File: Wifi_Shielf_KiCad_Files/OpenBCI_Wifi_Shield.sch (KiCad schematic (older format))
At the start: 32 parts, among them P1 CONN_01X04, P10 CONN_01X04, P2 CONN_01X04, P4 CONN_01X02, P5 CONN_01X02, P6 CONN_01X02, P7 CONN_01X08, P8 CONN_01X08, P9 CONN_01X04, SW1 TACT_SWITCH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

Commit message: Aproveitamento do ESP-12E
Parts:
- removed U3: ESP32-WROOM-32, RF_Module:ESP32-WROOM-32, symbol RF_Module:ESP32-WROOM-32
- added IC?: REF200AU, SOIC127P600X175-8N, symbol REF200AU:REF200AU
- added IC?: CD4066BE, DIP794W53P254L1930H508Q14N, symbol CD4066BE:CD4066BE
- added J?: Conn_4x1_HDTDCS, symbol Connector:Conn_01x05_Female
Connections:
- net GND: now also IC?.7 (VSS)
- net C_C: now reaches U1.13 (GPIO4)
- net C_C: now also IC?.6 (CONTROL_C)
- net C_A: now reaches U1.19 (GPIO9)
- net C_A: now also IC?.13 (CONTROL_A)
- net C_B: now reaches U1.20 (GPIO10)
- net C_B: now also IC?.5 (CONTROL_B)
- new net 9V: IC?.14 (VDD), IC?.4 (MIRROR_OUTPUT), IC?.7 (I2_HIGH), IC?.8 (I1_HIGH)
- new net A_OUT: IC?.2 (SIG_A_OUT/IN)
- new net B_OUT: IC?.4 (SIG_B_IN/OUT), IC?.5 (MIRROR_INPUT), IC?.8 (SIG_C_IN/OUT)
- new net COMM: IC?.3 (MIRROR_COMMON)
- new net I1: IC?.1 (I1_LOW), IC?.1 (SIG_A_IN/OUT), IC?.9 (SIG_C_OUT/IN)
- new net I2: IC?.2 (I2_LOW), IC?.3 (SIG_B_OUT/IN)
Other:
- note added: "CURRENT SOURCE"
- moved on the sheet: C1, C2, C3, C4, D1, D2, D3, D4, P1, P10, P2, P4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

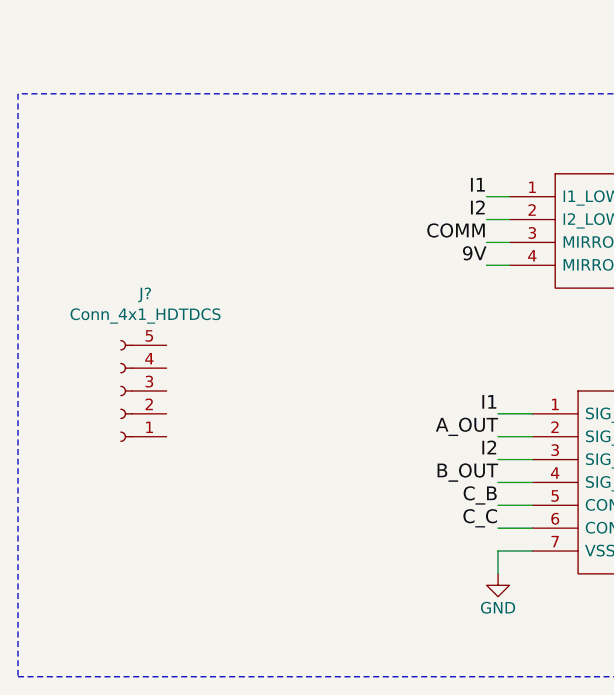
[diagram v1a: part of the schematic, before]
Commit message: Add dos conectores no esquemático de tdcs
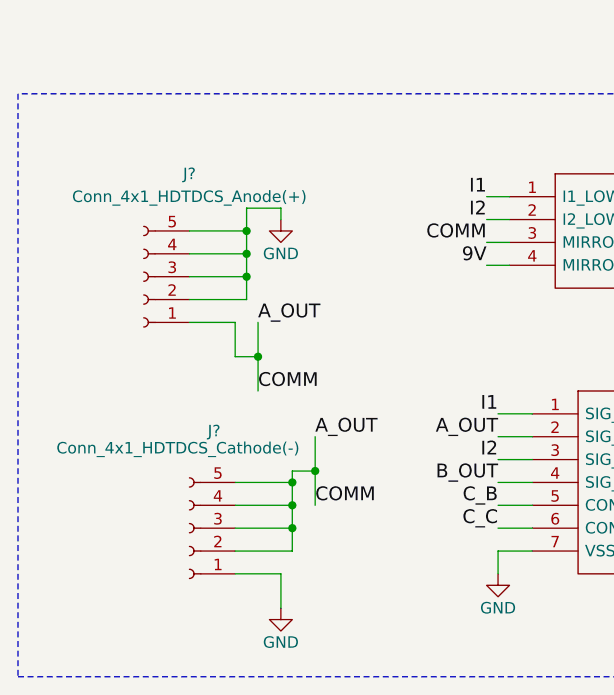
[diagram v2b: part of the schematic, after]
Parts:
- added J?: Conn_4x1_HDTDCS_Anode(+), symbol Connector:Conn_01x05_Female
- J?: value Conn_4x1_HDTDCS -> Conn_4x1_HDTDCS_Cathode(-)
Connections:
- net COMM is gone; now on net A_OUT: IC?.3 (MIRROR_COMMON)
- net A_OUT: now also J?.2 (Pin_2), J?.3 (Pin_3), J?.4 (Pin_4), J?.5 (Pin_5), J?.1 (Pin_1)
- net GND: now also J?.1 (Pin_1), J?.2 (Pin_2), J?.3 (Pin_3), J?.4 (Pin_4), J?.5 (Pin_5)
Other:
- moved on the sheet: J?
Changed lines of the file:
@@
 L Connector:Conn_01x05_Female J?
 U 1 1 631EBAD7
-P 4400 8550
-F 0 "J?" H 4292 8125 50  0000 C CNN
-F 1 "Conn_4x1_HDTDCS" H 4292 8216 50  0000 C CNN
-F 2 "" H 4400 8550 50  0001 C CNN
-F 3 "~" H 4400 8550 50  0001 C CNN
-	1    4400 8550
+P 4700 9150
+F 0 "J?" H 4592 8725 50  0000 C CNN
+F 1 "Conn_4x1_HDTDCS_Cathode(-)" H 4750 8800 50  0000 C CNN
+F 2 "" H 4700 9150 50  0001 C CNN
+F 3 "~" H 4700 9150 50  0001 C CNN
+	1    4700 9150
 	-1   0    0    1
 $EndComp
+$Comp
+L power:GND #PWR?
+U 1 1 6317ABCD
+P 5100 9500
+F 0 "#PWR?" H 5100 9250 50  0001 C CNN
+F 1 "GND" H 5100 9350 50  0000 C CNN
+F 2 "" H 5100 9500 50  0000 C CNN
+F 3 "" H 5100 9500 50  0000 C CNN
+	1    5100 9500
+	1    0    0    -1
+$EndComp
+Wire Wire Line
+	4900 9350 5100 9350
+Wire Wire Line
+	5100 9350 5100 9500
+Text Label 5250 8750 0    60   ~ 0
+A_OUT
+Text Label 5250 9050 0    60   ~ 0
+COMM
+Wire Wire Line
+	5150 8900 5250 8900
+Wire Wire Line
+	5250 8900 5250 8750
+Wire Wire Line
+	5250 9050 5250 8900
+Connection ~ 5250 8900
+Wire Wire Line
+	5150 9250 5150 9150
+Connection ~ 5150 9150
+Wire Wire Line
+	5150 9150 5150 9050
+Connection ~ 5150 9050
+Wire Wire Line
+	5150 9050 5150 8950
+Connection ~ 5150 8950
+Wire Wire Line
+	5150 8950 5150 8900
+Wire Wire Line
+	4900 9250 5150 9250
+Wire Wire Line
+	4900 9150 5150 9150
+Wire Wire Line
+	4900 9050 5150 9050
+Wire Wire Line
+	4900 8950 5150 8950
+$Comp
+L Connector:Conn_01x05_Female J?
+U 1 1 632256B4
+P 4500 8050
+F 0 "J?" H 4300 7600 50  0000 C CNN
+F 1 "Conn_4x1_HDTDCS_Anode(+)" H 4300 7700 50  0000 C CNN
+F 2 "" H 4500 8050 50  0001 C CNN
+F 3 "~" H 4500 8050 50  0001 C CNN
+	1    4500 8050
+	-1   0    0    1
+$EndComp
+$Comp
+L power:GND #PWR?
+U 1 1 632256BA
+P 5100 7800
+F 0 "#PWR?" H 5100 7550 50  0001 C CNN
+F 1 "GND" H 5100 7650 50  0000 C CNN
+F 2 "" H 5100 7800 50  0000 C CNN
+F 3 "" H 5100 7800 50  0000 C CNN
+	1    5100 7800
+	1    0    0    -1
+$EndComp
+Wire Wire Line
+	4700 8250 4900 8250
+Wire Wire Line
+	4900 8250 4900 8400
+Text Label 5000 8250 0    60   ~ 0
+A_OUT
+Text Label 5000 8550 0    60   ~ 0
+COMM
+Wire Wire Line
+	4900 8400 5000 8400
+Wire Wire Line
+	5000 8400 5000 8250
+Wire Wire Line
+	5000 8550 5000 8400
+Connection ~ 5000 8400
+Wire Wire Line
+	4950 8150 4950 8050
+Connection ~ 4950 8050
+Wire Wire Line
+	4950 8050 4950 7950
+Connection ~ 4950 7950
+Wire Wire Line
+	4950 7950 4950 7850
+Connection ~ 4950 7850
+Wire Wire Line
+	4700 8150 4950 8150
+Wire Wire Line
+	4700 8050 4950 8050
+Wire Wire Line
+	4700 7950 4950 7950
+Wire Wire Line
+	4700 7850 4950 7850
+Wire Wire Line
+	4950 7750 5100 7750
+Wire Wire Line
+	5100 7750 5100 7800
+Wire Wire Line
+	4950 7750 4950 7850
 $EndSCHEMATC

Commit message: Adição dos gerber files e layout da pcb
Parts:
- J? (x2): footprint (none) -> Connector_PinHeader_2.54mm:PinHeader_1x05_P2.54mm_Vertical
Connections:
- net 9V is gone; now on net 6V: IC?.14 (VDD), IC?.4 (MIRROR_OUTPUT), IC?.7 (I2_HIGH), IC?.8 (I1_HIGH)
- net 6V: now reaches R2.1, SW3.1 (T), U2.1 (IN)
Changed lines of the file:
@@
 $EndComp
 Wire Wire Line
-	6850 2300 7200 2300
+	6850 2300 7050 2300
 Wire Wire Line
 	8200 3550 8550 3550
@@
 COMM
 Text Label 6000 8000 2    60   ~ 0
-9V
+6V
 Text Label 8150 7500 0    60   ~ 0
-9V
+6V
 Wire Wire Line
 	8100 7800 8150 7800
@@
 	6050 8650 6200 8650
 Text Label 8250 8650 0    60   ~ 0
-9V
+6V
 Wire Wire Line
 	8100 8650 8250 8650
@@
 F 0 "J?" H 4592 8725 50  0000 C CNN
 F 1 "Conn_4x1_HDTDCS_Cathode(-)" H 4750 8800 50  0000 C CNN
-F 2 "" H 4700 9150 50  0001 C CNN
+F 2 "Connector_PinHeader_2.54mm:PinHeader_1x05_P2.54mm_Vertical" H 4700 9150 50  0001 C CNN
 F 3 "~" H 4700 9150 50  0001 C CNN
 	1    4700 9150
@@
 F 0 "J?" H 4300 7600 50  0000 C CNN
 F 1 "Conn_4x1_HDTDCS_Anode(+)" H 4300 7700 50  0000 C CNN
-F 2 "" H 4500 8050 50  0001 C CNN
+F 2 "Connector_PinHeader_2.54mm:PinHeader_1x05_P2.54mm_Vertical" H 4500 8050 50  0001 C CNN
 F 3 "~" H 4500 8050 50  0001 C CNN
 	1    4500 8050
@@
 Wire Wire Line
 	4950 7750 4950 7850
+Text Label 7050 2100 0    60   ~ 0
+6V
+Wire Wire Line
+	7050 2100 7050 2300
+Connection ~ 7050 2300
+Wire Wire Line
+	7050 2300 7200 2300
 $EndSCHEMATC

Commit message: Atualiazação do layout (3.3v conectado)
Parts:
- gave numbers to parts that had none: 4
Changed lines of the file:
@@
 	5150 5000 5250 5000
 $Comp
-L REF200AU:REF200AU IC?
+L REF200AU:REF200AU IC1
 U 1 1 6316B43A
 P 6100 7700
-F 0 "IC?" H 7100 7965 50  0000 C CNN
+F 0 "IC1" H 7100 7965 50  0000 C CNN
 F 1 "REF200AU" H 7100 7874 50  0000 C CNN
 F 2 "SOIC127P600X175-8N" H 7950 7800 50  0001 L CNN
@@
 $EndComp
 $Comp
-L CD4066BE:CD4066BE IC?
+L CD4066BE:CD4066BE IC2
 U 1 1 6316C4E8
 P 6200 8650
-F 0 "IC?" H 7150 8915 50  0000 C CNN
+F 0 "IC2" H 7150 8915 50  0000 C CNN
 F 1 "CD4066BE" H 7150 8824 50  0000 C CNN
 F 2 "DIP794W53P254L1930H508Q14N" H 7950 8750 50  0001 L CNN
@@
 C_C
 $Comp
-L power:GND #PWR?
+L power:GND #PWR024
 U 1 1 631942E9
 P 6050 9350
-F 0 "#PWR?" H 6050 9100 50  0001 C CNN
+F 0 "#PWR024" H 6050 9100 50  0001 C CNN
 F 1 "GND" H 6050 9200 50  0000 C CNN
 F 2 "" H 6050 9350 50  0000 C CNN
@@
 C_C
 $Comp
-L Connector:Conn_01x05_Female J?
+L Connector:Conn_01x05_Female J2
 U 1 1 631EBAD7
 P 4700 9150
-F 0 "J?" H 4592 8725 50  0000 C CNN
+F 0 "J2" H 4592 8725 50  0000 C CNN
 F 1 "Conn_4x1_HDTDCS_Cathode(-)" H 4750 8800 50  0000 C CNN
 F 2 "Connector_PinHeader_2.54mm:PinHeader_1x05_P2.54mm_Vertical" H 4700 9150 50  0001 C CNN
@@
 $EndComp
 $Comp
-L power:GND #PWR?
+L power:GND #PWR023
 U 1 1 6317ABCD
 P 5100 9500
-F 0 "#PWR?" H 5100 9250 50  0001 C CNN
+F 0 "#PWR023" H 5100 9250 50  0001 C CNN
 F 1 "GND" H 5100 9350 50  0000 C CNN
 F 2 "" H 5100 9500 50  0000 C CNN
@@
 	4900 8950 5150 8950
 $Comp
-L Connector:Conn_01x05_Female J?
+L Connector:Conn_01x05_Female J1
 U 1 1 632256B4
 P 4500 8050
-F 0 "J?" H 4300 7600 50  0000 C CNN
+F 0 "J1" H 4300 7600 50  0000 C CNN
 F 1 "Conn_4x1_HDTDCS_Anode(+)" H 4300 7700 50  0000 C CNN
 F 2 "Connector_PinHeader_2.54mm:PinHeader_1x05_P2.54mm_Vertical" H 4500 8050 50  0001 C CNN
@@
 $EndComp
 $Comp
-L power:GND #PWR?
+L power:GND #PWR022
 U 1 1 632256BA
 P 5100 7800
-F 0 "#PWR?" H 5100 7550 50  0001 C CNN
+F 0 "#PWR022" H 5100 7550 50  0001 C CNN
 F 1 "GND" H 5100 7650 50  0000 C CNN
 F 2 "" H 5100 7800 50  0000 C CNN
